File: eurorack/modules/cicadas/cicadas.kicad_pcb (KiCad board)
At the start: 2 copper layers, 42.6 x 128.5 mm, 79 parts, among them J1 Conn_02x05_Odd_Even, J10 AudioJack2_SwitchT, J11 AudioJack2_SwitchT, J2 AVR-ISP-6, J3 AudioJack2_SwitchT, J4 AudioJack2_SwitchT, J5 AudioJack2_SwitchT, J6 AudioJack2_SwitchT, J7 AudioJack2_SwitchT, J8 AudioJack2_SwitchT, J9 AudioJack2_SwitchT, U1 L78L33_SOT89, U2 ATmega328P-A, U3 MCP4822, U4 MCP4822

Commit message: initial work on cicadas v3
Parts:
- removed ? (x21): , 
- removed C2: 100n, Capacitor_SMD:C_0805_2012Metric_Pad1.18x1.45mm_HandSolder
- removed J2: AVR-ISP-6, Connector_PinHeader_2.54mm:PinHeader_2x03_P2.54mm_Vertical_SMD
- removed R2: R, Resistor_SMD:R_0805_2012Metric_Pad1.20x1.40mm_HandSolder
- removed TP1: 3.3V, TestPoint:TestPoint_Pad_D1.5mm
- removed TP10: B, TestPoint:TestPoint_Pad_D1.5mm
- removed TP11: A4, TestPoint:TestPoint_Pad_D1.5mm
- removed TP12: A3, TestPoint:TestPoint_Pad_D1.5mm
- removed TP13: GND, TestPoint:TestPoint_Pad_D1.5mm
- removed TP2: D4, TestPoint:TestPoint_Pad_D1.5mm
- removed TP3: D3, TestPoint:TestPoint_Pad_D1.5mm
- removed TP4: D2, TestPoint:TestPoint_Pad_D1.5mm
- removed TP5: A2, TestPoint:TestPoint_Pad_D1.5mm
- removed TP6: D1, TestPoint:TestPoint_Pad_D1.5mm
- removed TP7: A1, TestPoint:TestPoint_Pad_D1.5mm
- removed TP8: R, TestPoint:TestPoint_Pad_D1.5mm
- removed TP9: G, TestPoint:TestPoint_Pad_D1.5mm
- removed U2: ATmega328P-A, Package_QFP:TQFP-32_7x7mm_P0.8mm
- removed mouse-bite-2.54mm-slot: VAL**, Pale Slim Ghost:mousebite-2x5mm
- removed the mouse-bite-2mm-slot at (72.0, 68.8)
- added D10: SK6812MINI, Pale Slim Ghost:SK6812MINI-E, F.Cu at (58.7, 149.6)
- added D11: SK6812MINI, Pale Slim Ghost:SK6812MINI-E, F.Cu at (63.2, 149.6)
- added D5: SK6812MINI, Pale Slim Ghost:SK6812MINI-E, F.Cu at (63.2, 103.9)
- added D6: SK6812MINI, Pale Slim Ghost:SK6812MINI-E, F.Cu at (58.7, 119.1)
- added D7: SK6812MINI, Pale Slim Ghost:SK6812MINI-E, F.Cu at (63.2, 119.1)
- added D8: SK6812MINI, Pale Slim Ghost:SK6812MINI-E, F.Cu at (58.7, 134.4)
- added D9: SK6812MINI, Pale Slim Ghost:SK6812MINI-E, F.Cu at (63.2, 134.4)
- added H1: MountingHole, Pale Slim Ghost:eurorack panel mounting slot, F.Cu at (81.2, 46.2)
- added H10: MountingHole, Pale Slim Ghost:hole 6mm (jack panel), F.Cu at (78.2, 156.6)
- added H11: MountingHole, Pale Slim Ghost:hole 6mm (jack panel), F.Cu at (89.4, 156.6)
- added H12: MountingHole, Pale Slim Ghost:eurorack panel mounting slot, F.Cu at (81.2, 168.7)
- added H2: MountingHole, Pale Slim Ghost:hole 6mm (jack panel), F.Cu at (83.8, 58.0)
- added H3: MountingHole, Pale Slim Ghost:hole 9mm (encoder panel), F.Cu at (83.8, 84.8)
- added H4: MountingHole, Pale Slim Ghost:hole 6mm (jack panel), F.Cu at (78.2, 110.9)
- added H5: MountingHole, Pale Slim Ghost:hole 6mm (jack panel), F.Cu at (89.4, 110.9)
- added H6: MountingHole, Pale Slim Ghost:hole 6mm (jack panel), F.Cu at (78.2, 126.2)
- added H7: MountingHole, Pale Slim Ghost:hole 6mm (jack panel), F.Cu at (89.4, 126.2)
- added H8: MountingHole, Pale Slim Ghost:hole 6mm (jack panel), F.Cu at (78.2, 141.4)
- added H9: MountingHole, Pale Slim Ghost:hole 6mm (jack panel), F.Cu at (89.4, 141.4)
- added mouse-bite-2mm-slot: VAL**, Pale Slim Ghost:mousebite-2.54x5.08mm, F.Cu at (72.4, 144.1)
- added mouse-bite-2mm-slot: VAL**, Pale Slim Ghost:mousebite-2.54x5.08mm, F.Cu at (72.4, 68.6)
- D3: footprint LED_SMD:LED_0805_2012Metric_Pad1.15x1.40mm_HandSolder -> Diode_SMD:D_0805_2012Metric_Pad1.15x1.40mm_HandSolder
- D4: value LED -> SK6812MINI; footprint LED_SMD:LED_0805_2012Metric_Pad1.15x1.40mm_HandSolder -> Pale Slim Ghost:SK6812MINI-E; moved to F.Cu
- G***: moved to B.Cu
- J10, J11, J3, J4, J5, J6, J7, J8, J9: footprint AudioJacks:Jack_3.5mm_QingPu_WQP-PJ398SM_Vertical -> Pale Slim Ghost:Jack_3.5mm_QingPu_WQP-PJ398SM_Vertical
- U1: value L78L33_SOT89 -> ProMicro; footprint Package_TO_SOT_SMD:SOT-89-3 -> promicro:ProMicro-NoSilk
- moved G*** 64.8 mm to (60.7, 127.1), turned to 180 degrees
- moved J1 39.8 mm to (64.3, 97.8), turned to 90 degrees
- moved C4 32.8 mm to (55.5, 58.7), turned to 90 degrees
- moved D2 32.5 mm to (53.5, 98.3), turned to 0 degrees
- moved D1 31.9 mm to (53.5, 101.0), turned to 0 degrees
- moved D4 30.6 mm to (58.7, 103.9), turned to 90 degrees
- moved C1 25.5 mm to (54.0, 93.0), turned to -90 degrees
- moved C3 11.3 mm to (59.1, 90.0)
- moved C6 9.96 mm to (61.0, 146.1)
- moved C7 9.96 mm to (61.0, 115.6)
- moved R5 8.92 mm to (64.0, 74.7), turned to 90 degrees
- moved R8 8.67 mm to (60.9, 73.7)
- moved C5 8.51 mm to (62.9, 90.0), turned to 180 degrees
- moved G*** 7.85 mm to (83.8, 107.7)
- moved R3 7.20 mm to (57.9, 74.7), turned to 90 degrees
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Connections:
- D4 pad 1: GND -> +3V3
- U1 pad 1: +3V3 -> encoder A
- U1 pad 2: GND -> encoder B
- U1 pad 3: +12V -> GND
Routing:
- net GND: track 153.0 -> 5.81 mm, vias 3 -> 8
- net +12V: track 14.9 -> 51.0 mm
- net CS1: track 7.83 -> 41.4 mm, vias 0 -> 2
- net D4: track 66.6 -> 95.8 mm, vias 0 -> 1
- net encoder A: track 20.6 -> 47.4 mm
- net encoder B: track 14.3 -> 40.9 mm
- net D3: track 51.3 -> 77.8 mm, vias 0 -> 1
- net CS2: track 44.8 -> 69.4 mm, vias 2 -> 1
- net +3V3: track 28.9 -> 4.95 mm, vias 6 -> 4
- net clock in: track 44.3 -> 20.4 mm, vias 2 -> 0
- net LED: track 0.00 -> 22.1 mm
- net SCK: track 50.4 -> 69.0 mm, vias 3 -> 1
- net COPI: track 47.7 -> 66.2 mm, vias 3 -> 1
- net D1: track 23.4 -> 41.7 mm, vias 0 -> 1
- net D2: track 41.7 -> 59.7 mm, vias 0 -> 1
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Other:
- board size 42.6 x 128.5 mm -> 43.2 x 128.5 mm
- board text added: "Cicadas v3 April 2022"
- board text added: "either way ↓"
- board text removed: "AVR ISP"
- board text removed: "Cicadas v2.1 • November 2021"
- board text removed: "red stripe"
- board text removed: "← either way →"

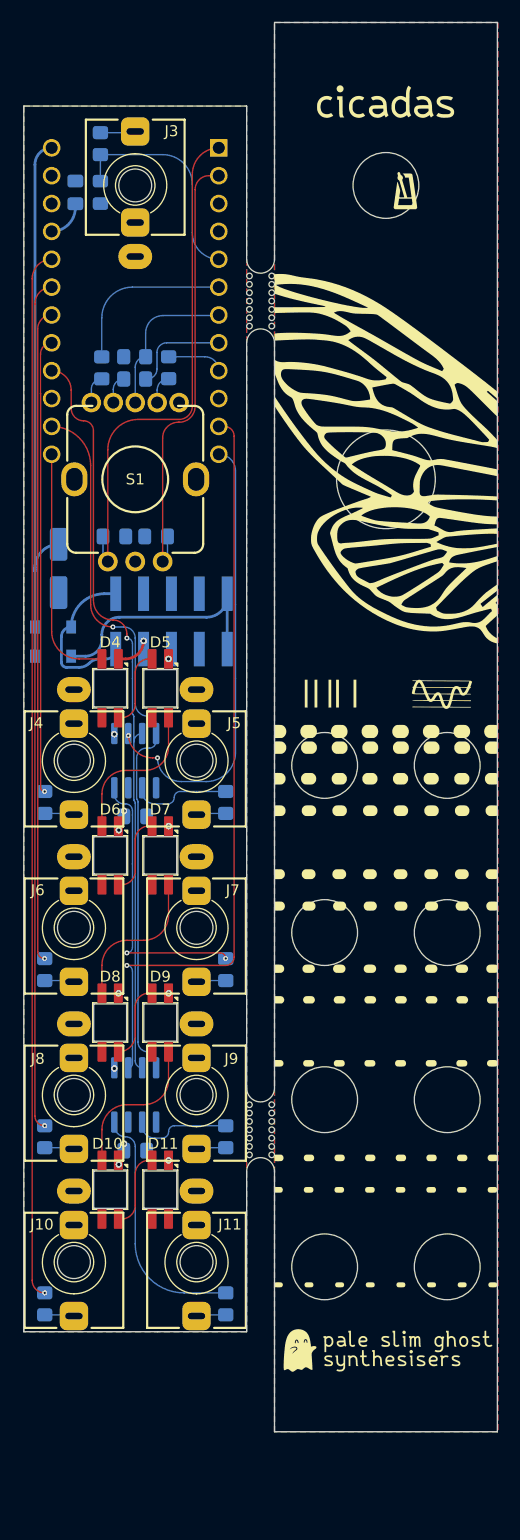
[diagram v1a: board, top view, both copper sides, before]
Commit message: add new art to cicadas board
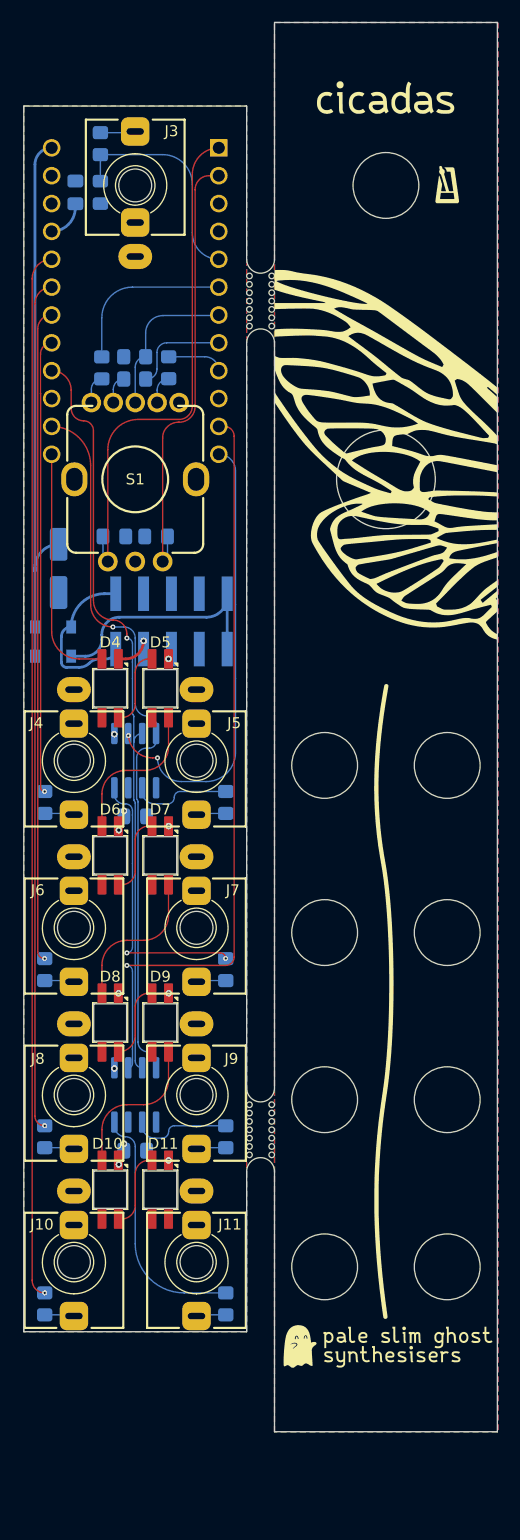
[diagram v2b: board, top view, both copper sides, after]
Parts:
- removed the G*** at (83.8, 107.7)
- added G***: LOGO, LOGO, F.Cu at (83.8, 107.3)
- added G***: LOGO, LOGO, F.Cu at (83.9, 107.5)

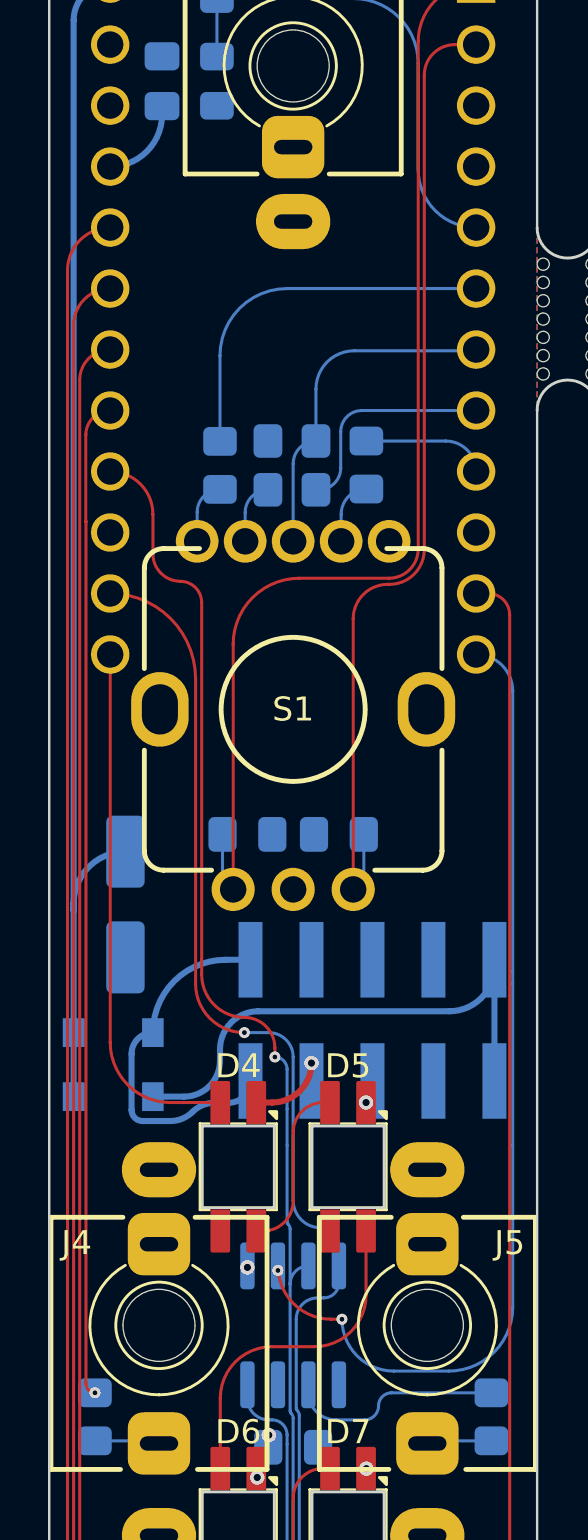
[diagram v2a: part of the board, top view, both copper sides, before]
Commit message: cicadas: normal clock input to 3v3 and fix missing ground connections
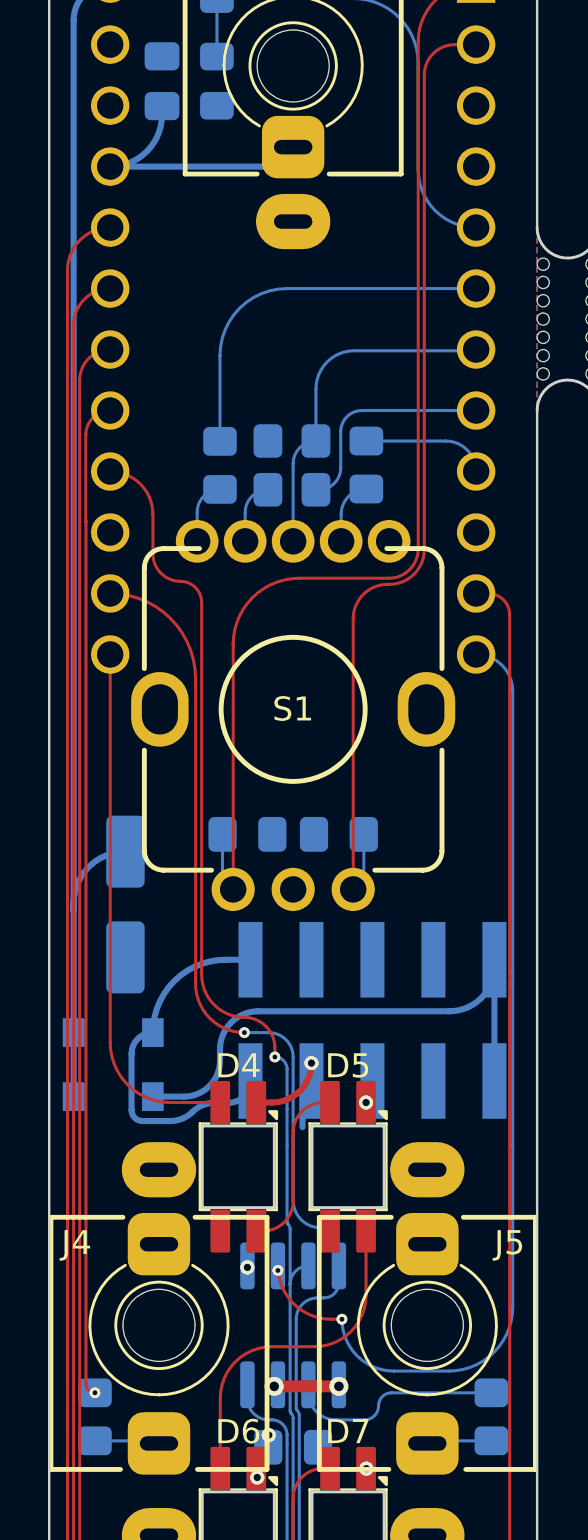
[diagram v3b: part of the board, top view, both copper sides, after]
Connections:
- J3 pad TN: unconnected-(J3-PadTN) -> +3V3
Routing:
- net +3V3: track 4.95 -> 13.0 mm
- net GND: track 5.81 -> 10.6 mm, vias 8 -> 10

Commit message: wip cicadas redesign
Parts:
- removed C4: 100n, Capacitor_SMD:C_0805_2012Metric_Pad1.18x1.45mm_HandSolder
- removed D1, D2: D, Diode_SMD:D_SOD-123
- removed J1: Conn_02x05_Odd_Even, Connector_PinHeader_2.54mm:PinHeader_2x05_P2.54mm_Vertical_SMD
- removed mouse-bite-2mm-slot (x2): VAL**, Pale Slim Ghost:mousebite-2.54x5.08mm
- added B1: Mousebite, Pale Slim Ghost:mousebite-2.54x5.08mm, F.Cu at (72.4, 68.6)
- added B2: Mousebite, Pale Slim Ghost:mousebite-2.54x5.08mm, F.Cu at (72.4, 144.1)
- added C2: 10u, Capacitor_SMD:C_0805_2012Metric_Pad1.18x1.45mm_HandSolder, B.Cu at (64.1, 95.9)
- added U2: Chordata, Pale Slim Ghost:Chordata, B.Cu at (61.0, 73.5)
- C1: footprint Capacitor_SMD:CP_Elec_5x4.5 -> Capacitor_SMD:C_0805_2012Metric_Pad1.18x1.45mm_HandSolder
- G1, G2: renamed from G***; value LOGO -> Artwork
- U1: value ProMicro -> MIC5219-5.0YM5; footprint promicro:ProMicro-NoSilk -> Package_TO_SOT_SMD:SOT-23-5
- moved U1 27.3 mm to (61.0, 95.9), turned to 0 degrees
- moved C1 4.80 mm to (57.8, 95.9)
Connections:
- C6 pad 1: +3V3 -> +5V
- C7 pad 1: +3V3 -> +5V
- D10 pad 1: +3V3 -> +5V
- D11 pad 1: +3V3 -> +5V
- D4 pad 1: +3V3 -> +5V
- D5 pad 1: +3V3 -> +5V
- D6 pad 1: +3V3 -> +5V
- D7 pad 1: +3V3 -> +5V
- D8 pad 1: +3V3 -> +5V
- D9 pad 1: +3V3 -> +5V
- U1 pad 1: encoder A -> +12V
- U1 pad 2: encoder B -> GND
- U1 pad 3: GND -> +12V
- U1 pad 4: GND -> unconnected-(U1-Pad4)
- U1 pad 5: clock in -> +5V
- U3 pad 1: +3V3 -> +5V
- U4 pad 1: +3V3 -> +5V
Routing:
- net +12V: track 51.0 -> 12.4 mm
- net encoder A: track 47.4 -> 15.8 mm
- net D4: track 95.8 -> 70.6 mm
- net Net-(D1-Pad2): track 23.7 -> 0.00 mm
- net encoder B: track 40.9 -> 20.1 mm
- net D3: track 77.8 -> 58.0 mm
- net Net-(D2-Pad2): track 15.2 -> 0.00 mm
- net D2: track 59.7 -> 45.3 mm
- net +3V3: track 13.0 -> 0.00 mm, vias 4 -> 0
- net LED B: track 5.25 -> 16.3 mm
- net clock in: track 20.4 -> 9.88 mm
- net LED R: track 15.7 -> 6.44 mm
- net D1: track 41.7 -> 32.6 mm
- net LED: track 22.1 -> 30.1 mm
- net CS2: track 69.4 -> 62.0 mm, vias 1 -> 0
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- added copper zone on F.Cu, net +5V
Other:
- board text added: "Cicadas v3.1 July 2022"
- board text removed: "Cicadas v3 April 2022"
- board text removed: "either way ↓"

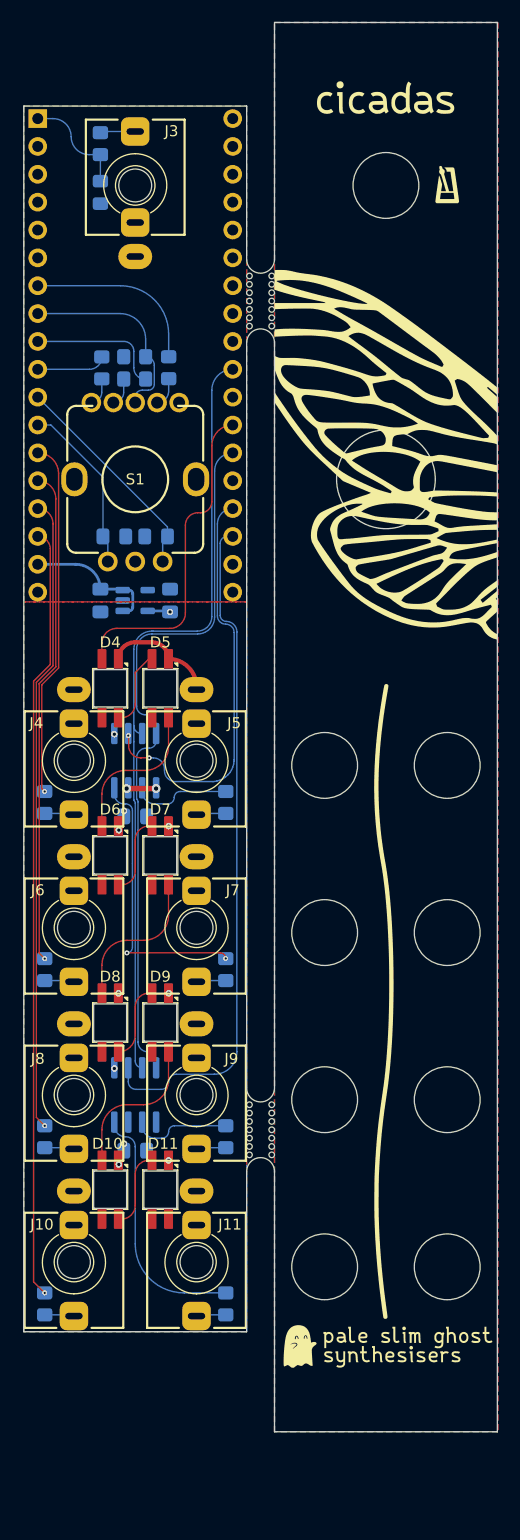
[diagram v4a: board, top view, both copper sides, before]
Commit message: cicadas panel with new branding
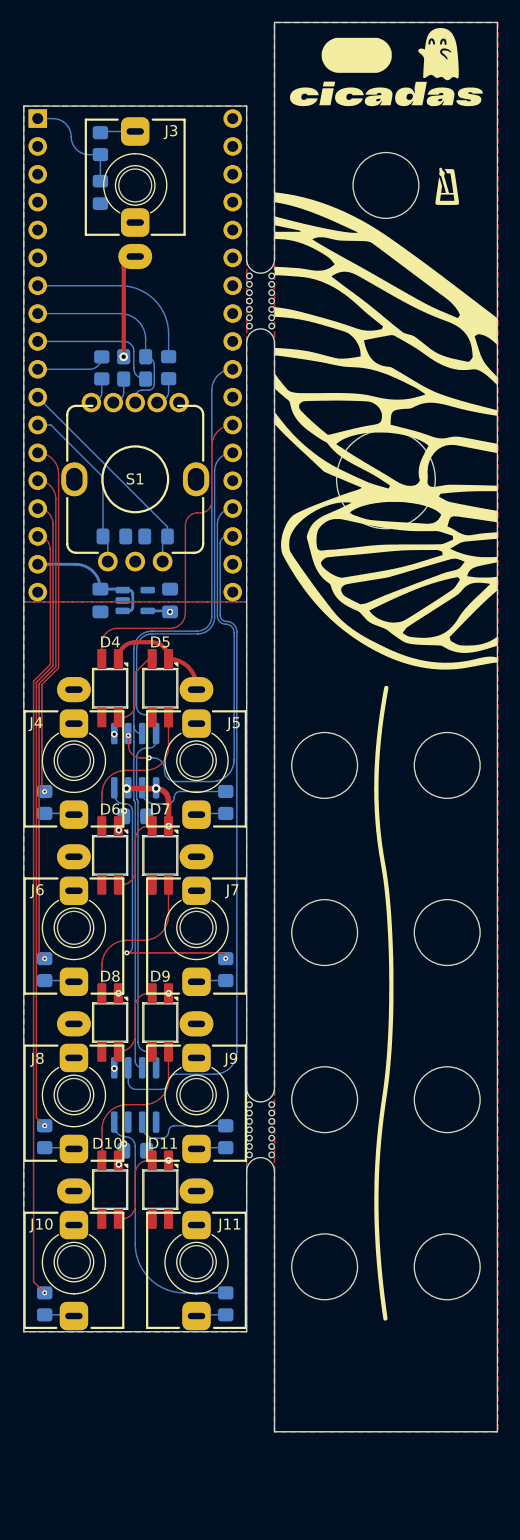
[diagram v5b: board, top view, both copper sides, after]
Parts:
- G2: value Artwork -> LOGO
- moved G2 0.16 mm to (83.8, 107.5)
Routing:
- net GND: track 14.4 -> 28.1 mm, vias 8 -> 9

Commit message: assorted changes ig from opening things in kicad 7
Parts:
- removed D10, D11, D4, D5, D6, D7, D8, D9: SK6812MINI, Pale Slim Ghost:SK6812MINI-E
- moved U2 0.13 mm to (61.0, 73.7)
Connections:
- U2 pad 25: LED -> unconnected-(U2-Pad25)
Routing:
- net LED: track 30.1 -> 0.00 mm
- net GND: track 28.1 -> 9.70 mm, vias 9 -> 1
- net Net-(D5-Pad2): track 13.9 -> 0.00 mm
- net Net-(D10-Pad4): track 13.8 -> 0.00 mm
- net Net-(D7-Pad2): track 13.8 -> 0.00 mm
- net Net-(D8-Pad2): track 7.33 -> 0.00 mm
- net Net-(D10-Pad2): track 7.25 -> 0.00 mm
- net Net-(D6-Pad2): track 7.25 -> 0.00 mm
- net Net-(D4-Pad2): track 7.11 -> 0.00 mm
